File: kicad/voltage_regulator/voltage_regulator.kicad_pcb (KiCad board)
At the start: 2 copper layers, 101 x 63.5 mm, 20 parts

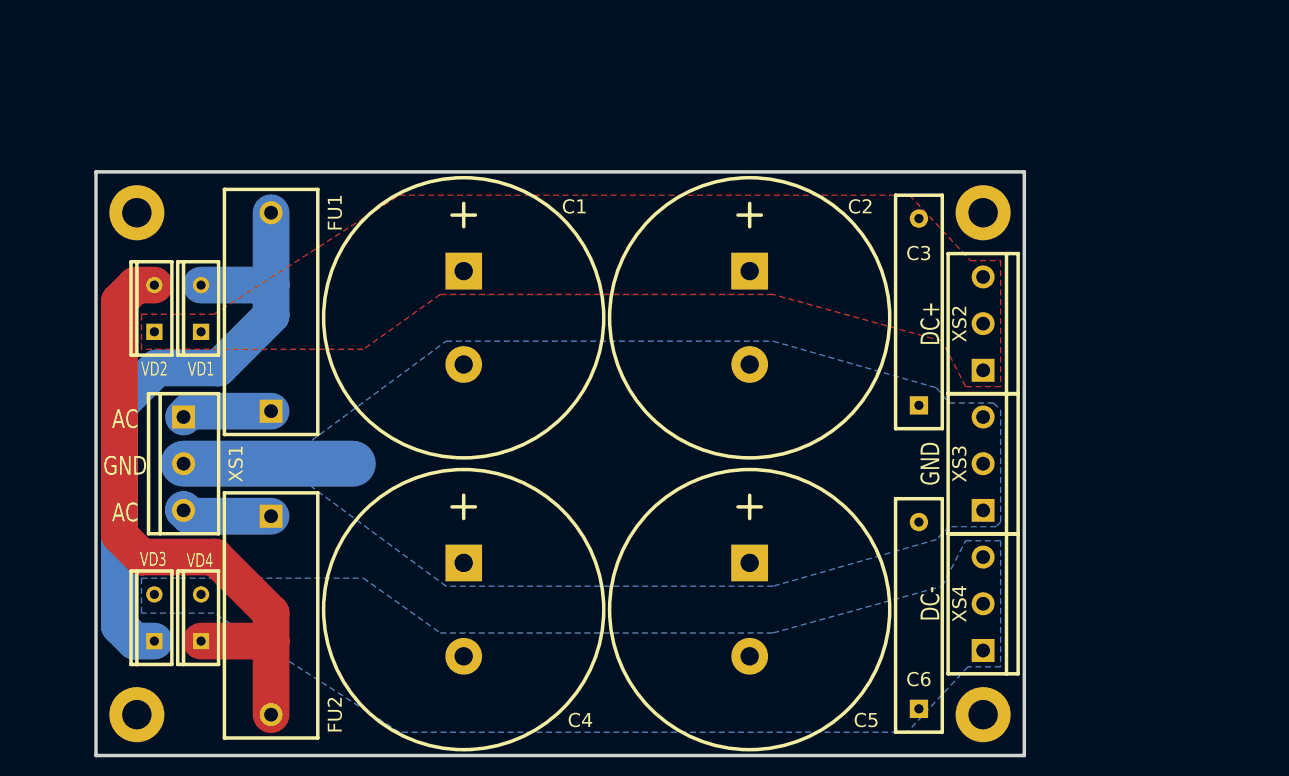
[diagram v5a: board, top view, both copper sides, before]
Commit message: Moved to kicad 4.0.0
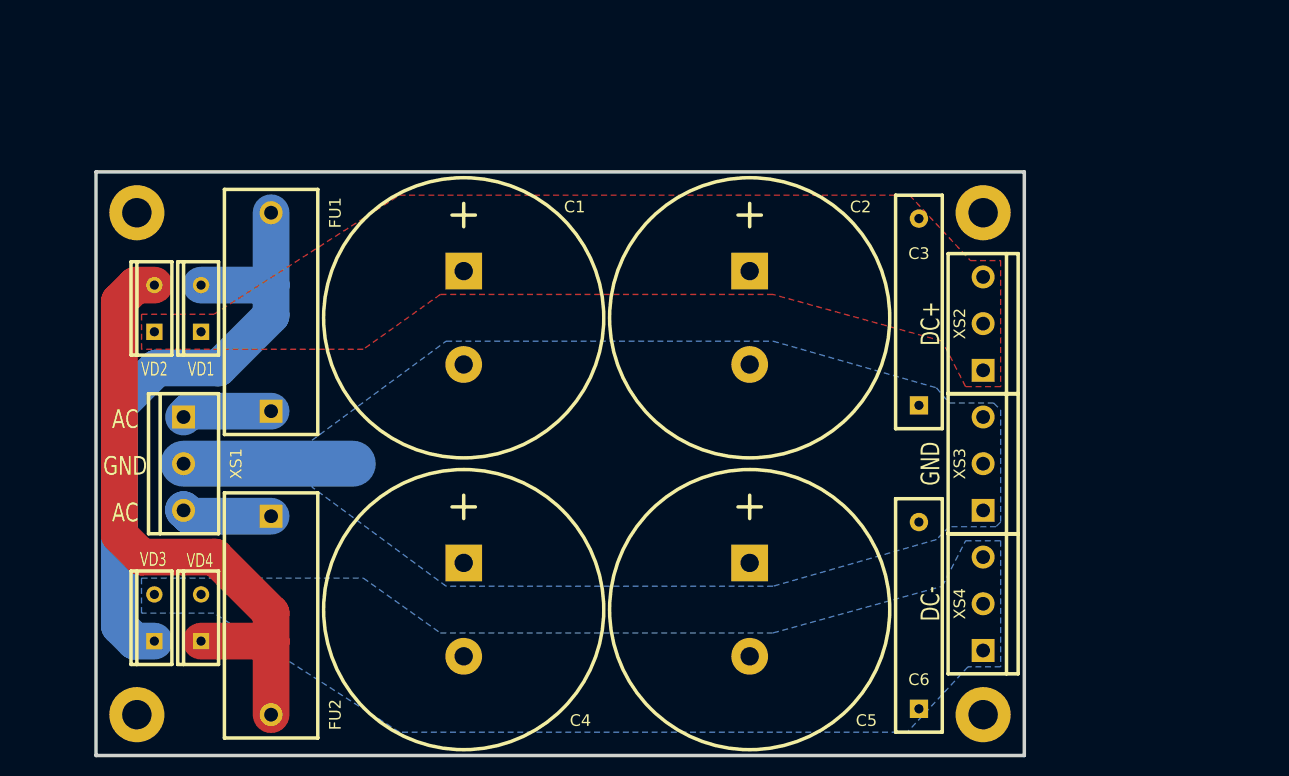
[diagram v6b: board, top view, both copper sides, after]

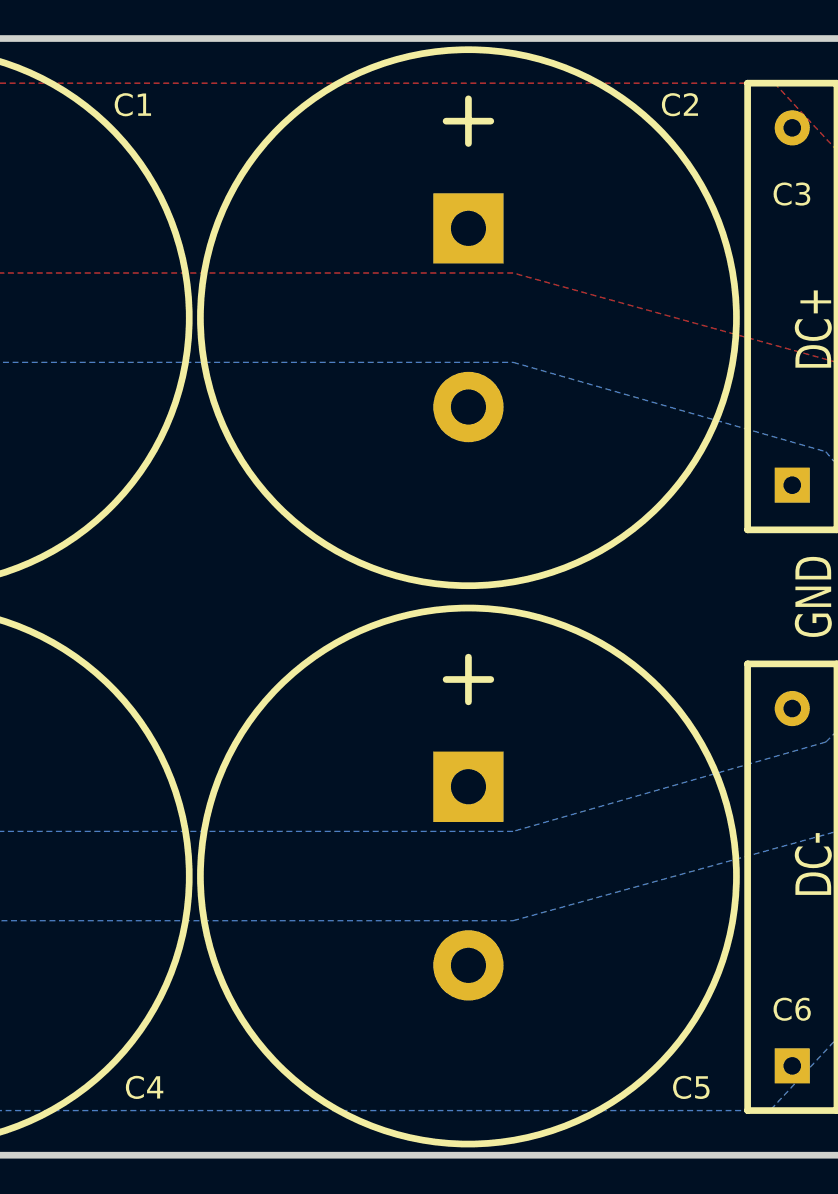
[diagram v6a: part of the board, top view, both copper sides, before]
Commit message: Add description to the schemes.
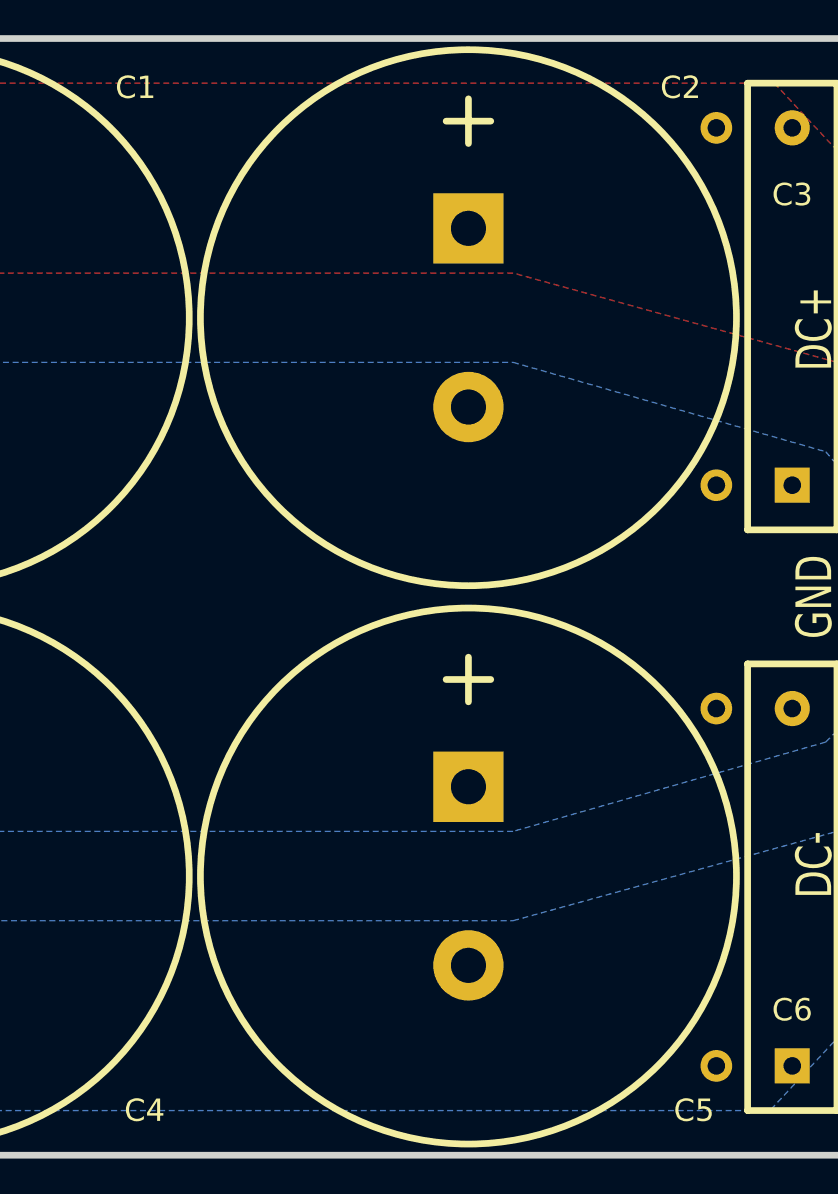
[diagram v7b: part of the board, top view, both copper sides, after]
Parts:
- added R1: 20 к, LFcomponents:RESISTOR_1W, B.Cu at (167.1, 80.0)
- added R2: 20 к, LFcomponents:RESISTOR_1W, B.Cu at (167.1, 113.0)
- C1, C2, C4, C5: value 10000 мк 63 В -> 10000 мк 50 В
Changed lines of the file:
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@@
-(kicad_pcb (version 4) (host pcbnew 4.0.1-2.201512121406+6195~38~ubuntu15.10.1-stable)
+(kicad_pcb (version 4) (host pcbnew 4.0.1-3.201512221401+6198~38~ubuntu15.10.1-stable)
   (general
-    (links 29)
+    (links 33)
     (no_connects 0)
-    (area 81.724499 64.579499 183.105501 128.460501)
+    (area 73.903858 61.955044 185.2342 128.460501)
     (thickness 1.6002)
     (drawings 10)
     (tracks 24)
     (zones 0)
-    (modules 20)
+    (modules 22)
     (nets 8)
   )
@@
       (drillshape 0)
       (scaleselection 1)
-      (outputdirectory ../../../../Документы/GERBER_power_supply_dv50a10/))
+      (outputdirectory /home/vdn/git/IWProject/kicad/voltage_regulator/))
   )
   (net 0 "")
@@
     (descr "Bornier d'alimentation 2 pins")
     (tags DEV)
-    (fp_text reference C4 (at 12.065 -12.7 360) (layer F.SilkS)
-      (effects (font (thickness 0.3048)))
-    )
-    (fp_text value "10000 мк 63 В" (at 0 17.78 270) (layer F.SilkS) hide
+    (fp_text reference C4 (at 13.335 -12.7 360) (layer F.SilkS)
+      (effects (font (thickness 0.3048)))
+    )
+    (fp_text value "10000 мк 50 В" (at 0 17.78 270) (layer F.SilkS) hide
       (effects (font (thickness 0.3048)))
     )
@@
     (descr "Bornier d'alimentation 2 pins")
     (tags DEV)
-    (fp_text reference C5 (at 12.065 -12.7 360) (layer F.SilkS)
-      (effects (font (thickness 0.3048)))
-    )
-    (fp_text value "10000 мк 63 В" (at 0 17.78 270) (layer F.SilkS) hide
+    (fp_text reference C5 (at 13.335 -12.827 360) (layer F.SilkS)
+      (effects (font (thickness 0.3048)))
+    )
+    (fp_text value "10000 мк 50 В" (at 0 17.78 270) (layer F.SilkS) hide
       (effects (font (thickness 0.3048)))
     )
@@
     (descr "Bornier d'alimentation 2 pins")
     (tags DEV)
-    (fp_text reference C1 (at -12.065 -12.065 360) (layer F.SilkS)
-      (effects (font (thickness 0.3048)))
-    )
-    (fp_text value "10000 мк 63 В" (at 0 17.78 270) (layer F.SilkS) hide
+    (fp_text reference C1 (at -13.081 -12.192 360) (layer F.SilkS)
+      (effects (font (thickness 0.3048)))
+    )
+    (fp_text value "10000 мк 50 В" (at 0 17.78 270) (layer F.SilkS) hide
       (effects (font (thickness 0.3048)))
     )
@@
     (descr "Bornier d'alimentation 2 pins")
     (tags DEV)
-    (fp_text reference C2 (at -12.065 -12.065 360) (layer F.SilkS)
-      (effects (font (thickness 0.3048)))
-    )
-    (fp_text value "10000 мк 63 В" (at 0 17.78 270) (layer F.SilkS) hide
+    (fp_text reference C2 (at -13.081 -12.065 360) (layer F.SilkS)
+      (effects (font (thickness 0.3048)))
+    )
+    (fp_text value "10000 мк 50 В" (at 0 17.78 270) (layer F.SilkS) hide
       (effects (font (thickness 0.3048)))
     )
@@
     )
   )
+  (module LFcomponents:RESISTOR_1W (layer Back)
+    (at 167.132 80.01 270)
+    (descr "Bornier d'alimentation 2 pins")
+    (tags DEV)
+    (fp_text reference R1 (at 0 4.445 270) (layer B.SilkS)
+      (effects (font (thickness 0.3048)) (justify mirror))
+    )
+    (fp_text value "20 к" (at 0 -4.445 270) (layer B.SilkS) hide
+      (effects (font (thickness 0.3048)) (justify mirror))
+    )
+    (fp_line (start -5.08 0) (end -8.89 0) (layer B.SilkS) (width 0.3048))
+    (fp_line (start 5.08 0) (end 8.89 0) (layer B.SilkS) (width 0.3048))
+    (fp_line (start -5.08 -2.54) (end 5.08 -2.54) (layer B.SilkS) (width 0.3048))
+    (fp_line (start 5.08 -2.54) (end 5.08 2.54) (layer B.SilkS) (width 0.3048))
+    (fp_line (start -5.08 -2.54) (end -5.08 2.54) (layer B.SilkS) (width 0.3048))
+    (fp_line (start -5.08 2.54) (end 5.08 2.54) (layer B.SilkS) (width 0.3048))
+    (pad 1 thru_hole circle (at -10.16 0 270) (size 1.8 1.8) (drill 1) (layers *.Cu *.Mask B.SilkS)
+      (net 2 /VCC+))
+    (pad 2 thru_hole circle (at 10.16 0 270) (size 1.8 1.8) (drill 1) (layers *.Cu *.Mask B.SilkS)
+      (net 1 /GND))
+  )
+  (module LFcomponents:RESISTOR_1W (layer Back)
+    (at 167.132 113.03 270)
+    (descr "Bornier d'alimentation 2 pins")
+    (tags DEV)
+    (fp_text reference R2 (at 0 4.445 270) (layer B.SilkS)
+      (effects (font (thickness 0.3048)) (justify mirror))
+    )
+    (fp_text value "20 к" (at 0 -4.445 270) (layer B.SilkS) hide
+      (effects (font (thickness 0.3048)) (justify mirror))
+    )
+    (fp_line (start -5.08 0) (end -8.89 0) (layer B.SilkS) (width 0.3048))
+    (fp_line (start 5.08 0) (end 8.89 0) (layer B.SilkS) (width 0.3048))
+    (fp_line (start -5.08 -2.54) (end 5.08 -2.54) (layer B.SilkS) (width 0.3048))
+    (fp_line (start 5.08 -2.54) (end 5.08 2.54) (layer B.SilkS) (width 0.3048))
+    (fp_line (start -5.08 -2.54) (end -5.08 2.54) (layer B.SilkS) (width 0.3048))
+    (fp_line (start -5.08 2.54) (end 5.08 2.54) (layer B.SilkS) (width 0.3048))
+    (pad 1 thru_hole circle (at -10.16 0 270) (size 1.8 1.8) (drill 1) (layers *.Cu *.Mask B.SilkS)
+      (net 1 /GND))
+    (pad 2 thru_hole circle (at 10.16 0 270) (size 1.8 1.8) (drill 1) (layers *.Cu *.Mask B.SilkS)
+      (net 3 /VCC-))
+  )
   (gr_line (start 182.915 64.77) (end 81.915 64.77) (angle 90) (layer Edge.Cuts) (width 0.381))
